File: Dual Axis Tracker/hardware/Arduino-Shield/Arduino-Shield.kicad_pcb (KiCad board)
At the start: 2 copper layers, 37.8 x 53.1 mm, 8 parts, among them J1 SERVO, J2 SERVO, J3 TO LDR BOARD, U1 ARDUINO

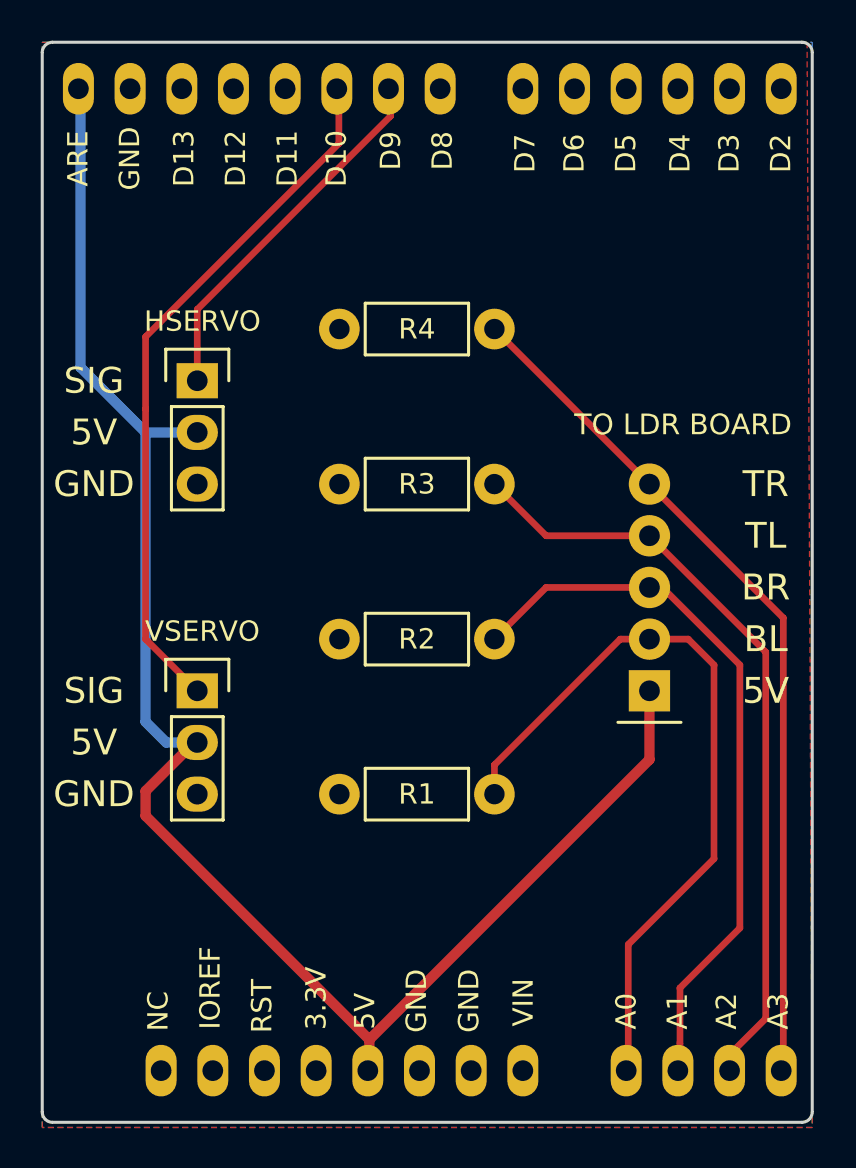
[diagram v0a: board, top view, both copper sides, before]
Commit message: Increased resistor length, v1.1 Arduino Shield
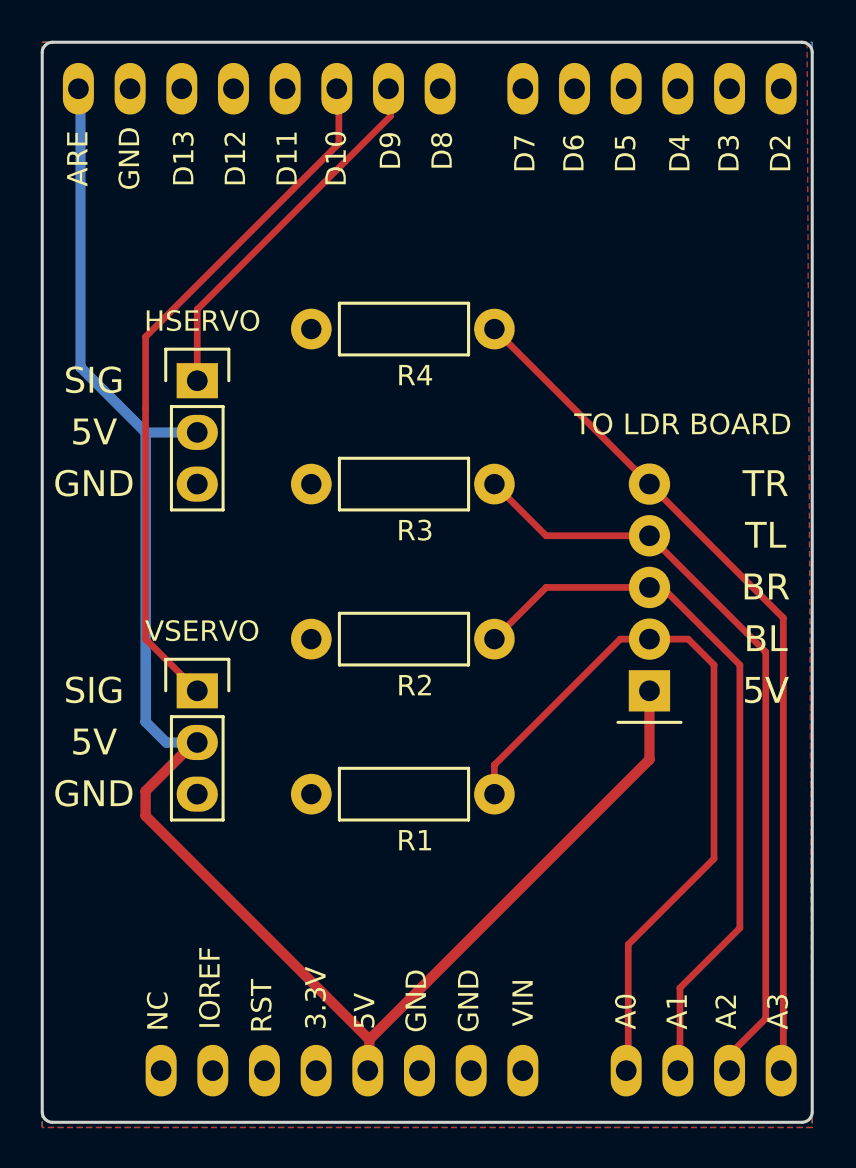
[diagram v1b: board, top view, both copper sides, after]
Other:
- board text added: "Solar Shield v1.1"
- board text added: "Solar Tracker Shield v1.1"
- board text removed: "Solar Shield v1.0"
- board text removed: "Solar Tracker Shield v1.0"
